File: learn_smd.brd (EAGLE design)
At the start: 27.9 x 34.3 mm, 11 parts, among them Q1 MMBT2222A, Q2 MMBT2222A

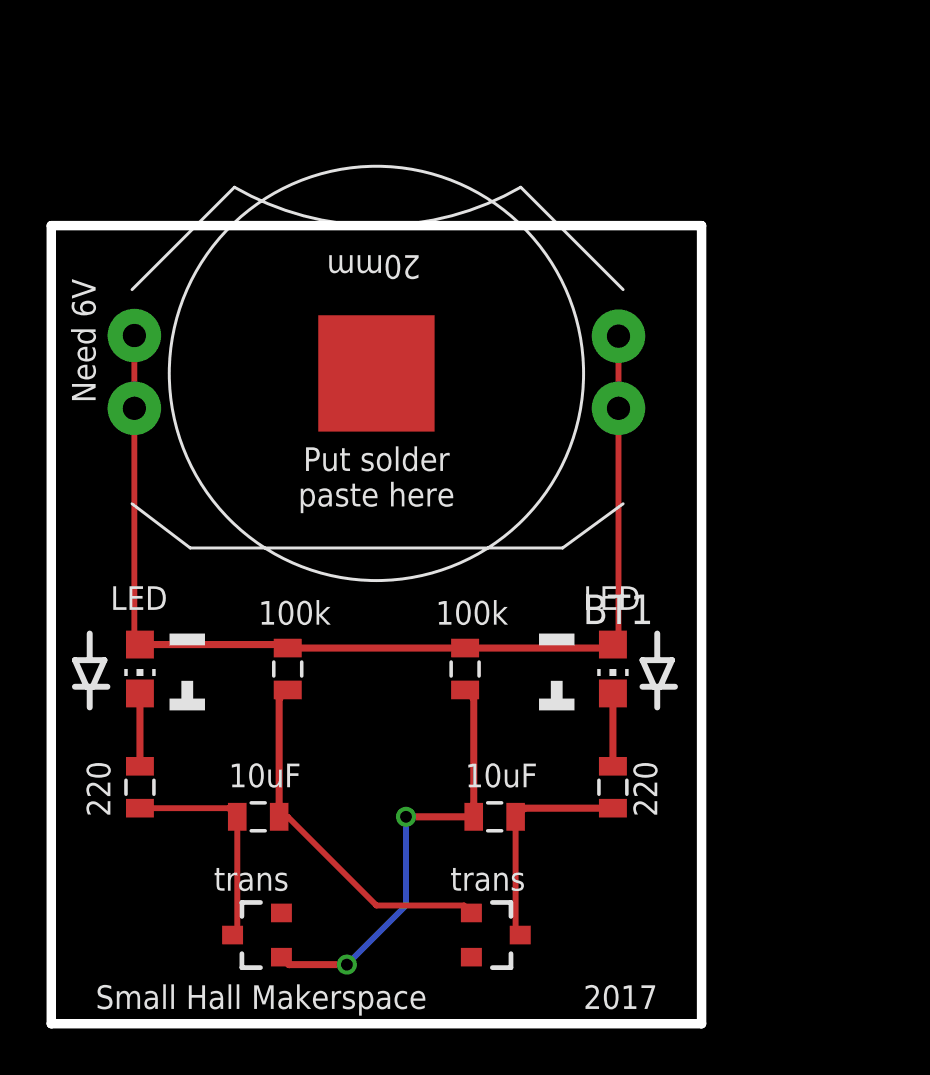
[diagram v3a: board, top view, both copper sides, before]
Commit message: made board smaller
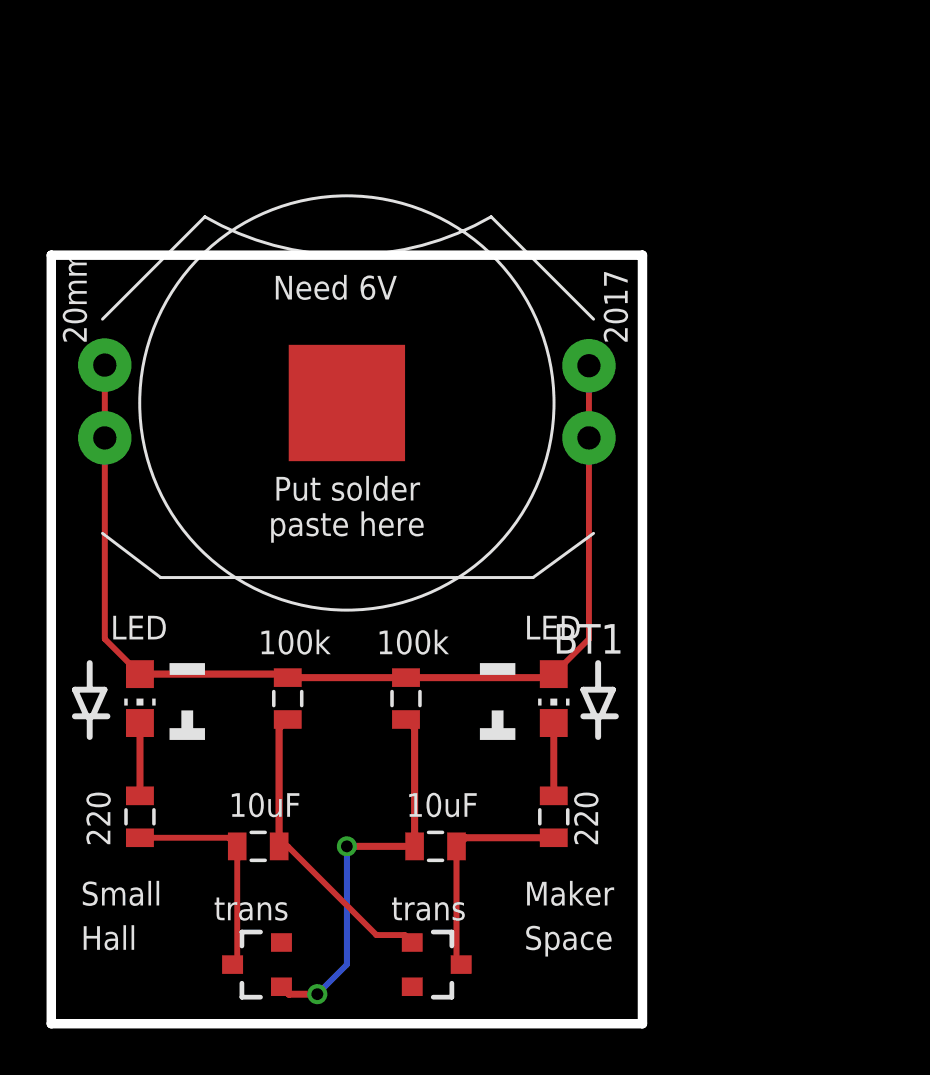
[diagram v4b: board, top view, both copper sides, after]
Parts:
- moved R4 2.84 mm to (15.2, 14.0)
- moved C1 2.84 mm to (16.5, 7.62)
- moved LED2 2.84 mm to (21.6, 14.0)
- moved Q2 2.84 mm to (16.5, 2.54)
- moved R2 2.84 mm to (21.6, 8.89)
- moved BT1 1.80 mm to (12.7, 26.7)
- moved C2 1.27 mm to (8.89, 7.62)
- moved Q1 1.27 mm to (8.89, 2.54)
- moved LED1 1.27 mm to (3.81, 14.0)
- moved R1 1.27 mm to (3.81, 8.89)
- moved R3 1.27 mm to (10.2, 14.0)
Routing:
- net N$7: track 15.6 -> 13.0 mm
- net N$3: track 18.9 -> 17.1 mm
- net N$6: track 47.3 -> 46.5 mm
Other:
- board size 27.9 x 34.3 mm -> 25.4 x 33 mm
- board text added: "Hall"
- board text added: "Maker"
- board text added: "Small"
- board text added: "Space"
- board text removed: "Small Hall Makerspace"
